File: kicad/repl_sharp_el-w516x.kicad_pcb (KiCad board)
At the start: 2 copper layers, 68.6 x 141.2 mm, 117 parts, among them J1 USB_B_Micro, J3 AVR-ISP-6, SW1 SW_RESET, SW10 SW_Push, SW11 SW_Push, SW12 SW_Push, SW13 SW_Push, SW14 SW_Push, SW15 SW_Push, SW16 SW_Push, SW17 SW_Push, SW18 SW_Push, SW19 SW_Push, SW2 SW_Push, SW20 SW_Push, SW21 SW_Push, SW22 SW_Push, SW23 SW_Push, SW24 SW_Push, SW25 SW_Push, SW26 SW_Push, SW27 SW_Push, SW28 SW_Push, SW29 SW_Push, SW3 SW_Push, SW30 SW_Push, SW31 SW_Push, SW32 SW_Push, SW33 SW_Push, SW34 SW_Push, SW35 SW_Push, SW36 SW_Push, SW37 SW_Push, SW38 SW_Push, SW39 SW_Push, SW4 SW_Push, SW40 SW_Push, SW41 SW_Push, SW42 SW_Push, SW43 SW_Push, SW44 SW_Push, SW45 SW_Push, SW46 SW_Push, SW47 SW_Push, SW48 SW_Push, SW49 SW_Push, SW5 SW_Push, SW50 SW_Push, SW51 SW_Push, SW52 SW_Push, SW53 SW_Push, SW58 SW_POWER, SW6 SW_Push, SW7 SW_Push, SW8 SW_Push, SW9 SW_Push, U1 74HC165D, U2 ATmega32U4-AU, U3 74HC595, U4 BQ24072RGTR, U5 AP2210-33, Y1 Crystal

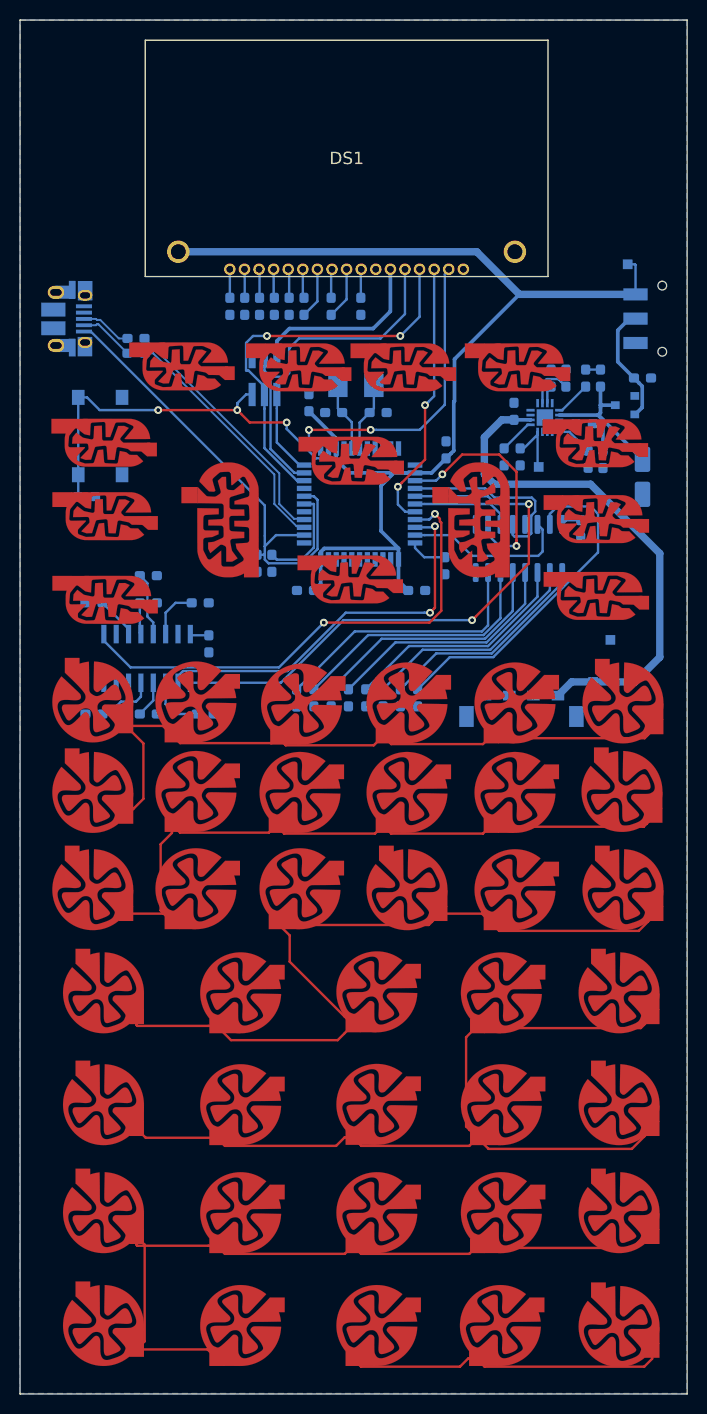
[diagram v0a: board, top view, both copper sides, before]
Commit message: kicad: completed partial layout
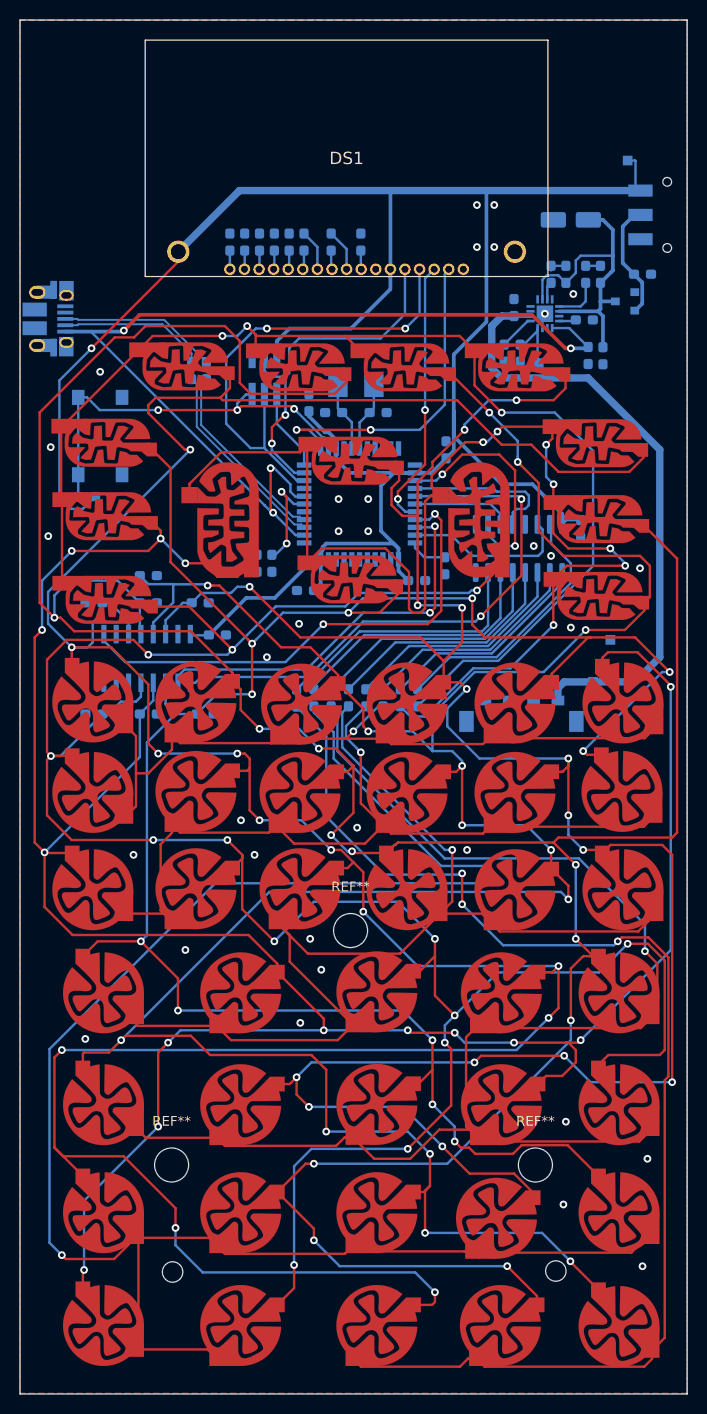
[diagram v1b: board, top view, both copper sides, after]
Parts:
- added REF**: MountingHole_2.1mm, MountingHole:MountingHole_2.1mm, F.Cu at (117.0, 137.5)
- added REF**: MountingHole_3.5mm, MountingHole:MountingHole_3.5mm, F.Cu at (135.3, 102.4)
- added REF**: MountingHole_3.5mm, MountingHole:MountingHole_3.5mm, F.Cu at (116.9, 126.5)
- added REF**: MountingHole_3.5mm, MountingHole:MountingHole_3.5mm, F.Cu at (154.3, 126.5)
- added REF**: MountingHole_2.1mm, MountingHole:MountingHole_2.1mm, F.Cu at (156.4, 137.4)
- moved C22 27.4 mm to (157.9, 29.3), turned to 180 degrees
- moved SW58 10.7 mm to (167.8, 28.8)
- moved C11 10.7 mm to (159.7, 43.3)
- moved C13 10.7 mm to (152.1, 38.4)
- moved C23 10.7 mm to (161.2, 43.3)
- moved C24 10.7 mm to (165.3, 34.9)
- moved D1 10.7 mm to (157.4, 34.9)
- moved D59 10.7 mm to (161.0, 34.9)
- moved R14 10.7 mm to (152.7, 43.0)
- moved R15 10.7 mm to (159.3, 39.6)
- moved R16 10.7 mm to (151.1, 43.0)
- moved R17 10.7 mm to (155.9, 34.9)
- moved R18 10.7 mm to (159.5, 34.9)
- moved TP1 10.7 mm to (163.8, 23.2)
- moved TP5 10.7 mm to (154.6, 44.1)
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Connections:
- net Net-(R2-Pad1) renamed /uD+
- net Net-(R3-Pad1) renamed /uD-
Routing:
- net row0: track 4.32 -> 307.6 mm, vias 0 -> 12
- net row1: track 3.26 -> 292.6 mm, vias 0 -> 11
- net row2: track 6.58 -> 270.8 mm, vias 0 -> 14
- net row5: track 3.79 -> 251.8 mm, vias 0 -> 14
- net row6: track 6.12 -> 245.0 mm, vias 0 -> 13
- net row3: track 5.30 -> 230.8 mm, vias 0 -> 15
- net row4: track 5.81 -> 217.2 mm, vias 0 -> 11
- net Net-(D3-Pad1): track 0.00 -> 128.1 mm, vias 0 -> 7
- net Net-(D2-Pad1): track 0.00 -> 122.2 mm, vias 0 -> 3
- net Net-(D8-Pad1): track 76.8 -> 186.1 mm, vias 0 -> 1
- net Net-(D9-Pad1): track 33.0 -> 130.5 mm, vias 0 -> 3
- net +3V3: track 142.5 -> 227.7 mm, vias 0 -> 1
- net VBUS: track 54.2 -> 109.0 mm, vias 0 -> 4
- net Net-(D7-Pad1): track 87.1 -> 141.2 mm, vias 0 -> 1
- net Net-(D6-Pad1): track 79.4 -> 109.1 mm, vias 0 -> 1
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- added copper zone on F.Cu, net -BATT

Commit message: kicad: finalize design
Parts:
- removed the C14 at (124.4, 31.6)
- removed the C15 at (127.5, 31.6)
- removed the C16 at (136.4, 31.6)
- removed the C17 at (122.9, 31.6)
- removed the C18 at (125.9, 31.6)
- removed the C19 at (129.0, 31.6)
- removed the C20 at (130.5, 31.6)
- removed the C21 at (133.3, 31.6)
- removed the D1 at (157.4, 34.9)
- removed SW11, SW13, SW2: SW_Push, pcb_buttons:btn_rect
- removed SW20, SW27, SW29, SW48, SW49: SW_Push, pcb_buttons:btn_circular
- added C10: 1u, Capacitor_SMD:C_0603_1608Metric_Pad1.05x0.95mm_HandSolder, B.Cu at (133.9, 31.6)
- added C3: 0.1u, Capacitor_SMD:C_0603_1608Metric_Pad1.05x0.95mm_HandSolder, B.Cu at (125.0, 31.6)
- added C4: 0.1u, Capacitor_SMD:C_0603_1608Metric_Pad1.05x0.95mm_HandSolder, B.Cu at (128.1, 31.6)
- added C5: 1u, Capacitor_SMD:C_0603_1608Metric_Pad1.05x0.95mm_HandSolder, B.Cu at (137.0, 31.6)
- added C6: 0.1u, Capacitor_SMD:C_0603_1608Metric_Pad1.05x0.95mm_HandSolder, B.Cu at (123.5, 31.6)
- added C7: 0.1u, Capacitor_SMD:C_0603_1608Metric_Pad1.05x0.95mm_HandSolder, B.Cu at (126.6, 31.6)
- added C8: 0.1u, Capacitor_SMD:C_0603_1608Metric_Pad1.05x0.95mm_HandSolder, B.Cu at (129.6, 31.6)
- added C9: 1u, Capacitor_SMD:C_0603_1608Metric_Pad1.05x0.95mm_HandSolder, B.Cu at (131.1, 31.6)
- added D11: LED, Diode_SMD:D_0603_1608Metric_Pad1.05x0.95mm_HandSolder, B.Cu at (145.6, 48.7)
- added D9: LED_PGOOD, LED_SMD:LED_0603_1608Metric_Pad1.05x0.95mm_HandSolder, B.Cu at (156.4, 33.7)
- added G***: LOGO, pcb_buttons:board, F.Cu at (135.3, 94.9)
- added R12: 10k, Resistor_SMD:R_0603_1608Metric_Pad1.05x0.95mm_HandSolder, B.Cu at (107.7, 74.3)
- added R15: 1k, Resistor_SMD:R_0603_1608Metric_Pad1.05x0.95mm_HandSolder, B.Cu at (159.2, 34.9)
- added REF**: MountingHole_2.1mm, MountingHole:MountingHole_2.1mm, F.Cu at (152.8, 50.3)
- added REF**: MountingHole_2.1mm, MountingHole:MountingHole_2.1mm, F.Cu at (117.7, 49.8)
- added SW54: SW_Push, pcb_buttons:btn_circular, F.Cu at (152.1, 88.0)
- added SW55: SW_Push, pcb_buttons:btn_circular, F.Cu at (163.3, 88.0)
- added SW58: SW_Push, pcb_buttons:btn_circular, F.Cu at (108.7, 78.9)
- added SW59: SW_Push, pcb_buttons:btn_circular, F.Cu at (119.3, 78.9)
- added SW60: SW_Push, pcb_buttons:btn_circular, F.Cu at (130.0, 78.9)
- added SW61: SW_Push, pcb_buttons:btn_circular, F.Cu at (140.9, 78.9)
- added SW62: SW_Push, pcb_buttons:btn_circular, F.Cu at (152.1, 78.9)
- added SW63: SW_Push, pcb_buttons:btn_circular, F.Cu at (163.3, 78.9)
- SW12: footprint pcb_buttons:btn_rect -> pcb_buttons:btn_long_rect
- SW14, SW15: footprint pcb_buttons:btn_long_rect -> pcb_buttons:btn_circular
- SW18, SW19, SW21, SW26, SW34, SW35, SW36, SW37: footprint pcb_buttons:btn_circular -> pcb_buttons:btn_rect
- SW28: footprint pcb_buttons:btn_circular -> pcb_buttons:btn_long_rect
- SW6, SW7, SW8, SW9: footprint pcb_buttons:btn_rect -> pcb_buttons:btn_circular
- moved SW9 104.0 mm to (109.9, 143.0), turned to 270 degrees
- moved SW34 77.5 mm to (152.9, 44.3), turned to 0 degrees
- moved SW35 67.5 mm to (161.0, 52.3)
- moved SW15 64.9 mm to (123.9, 120.3)
- moved SW17 64.3 mm to (123.9, 143.0), turned to 270 degrees
- moved SW8 63.0 mm to (109.9, 131.4), turned to 270 degrees
- moved SW7 60.5 mm to (109.9, 120.3), turned to 90 degrees
- moved SW53 59.3 mm to (140.9, 88.0), turned to 0 degrees
- moved SW52 58.6 mm to (130.0, 88.1)
- moved SW51 57.8 mm to (119.3, 88.3)
- moved SW50 56.9 mm to (108.8, 88.1)
- moved SW6 56.6 mm to (109.8, 108.8), turned to 270 degrees
- moved SW28 55.0 mm to (148.5, 60.2)
- moved SW25 54.8 mm to (137.9, 142.9), turned to 270 degrees
- moved SW16 54.7 mm to (123.9, 131.4), turned to 270 degrees
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- renumbered C2 to C1, C8 to C11, C9 to C13, C10 to C14, C1 to C15, C3 to C16, C5 to C17, C6 to C18, C13 to C19, C4 to C2, C22 to C20, C23 to C21, C11 to C22, C24 to C23, D2 to D1, D59 to D10, D3 to D2, D4 to D3, D5 to D4, D6 to D5, D7 to D6, D8 to D7, D9 to D8, J3 to J2, R11 to R10, R12 to R11, R16 to R13, R17 to R14, R14 to R16, R15 to R17, R5 to R4, R6 to R5, R7 to R6, R8 to R7, R9 to R8, R10 to R9, SW58 to SW66, TP4 to TP3, TP5 to TP4
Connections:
- C1 pad 2: -BATT -> GND
- C11 pad 2: -BATT -> GND
- C12 pad 1: -BATT -> GND
- C13 pad 2: -BATT -> GND
- C14 pad 1: -BATT -> GND
- C15 pad 2: -BATT -> GND
- C16 pad 2: -BATT -> GND
- C17 pad 2: -BATT -> GND
- C18 pad 2: -BATT -> GND
- C19 pad 1: -BATT -> GND
- C2 pad 2: -BATT -> GND
- C20 pad 2: -BATT -> GND
- C21 pad 2: -BATT -> GND
- C22 pad 1: -BATT -> GND
- C23 pad 2: -BATT -> GND
- D1 pad 1: Net-(D2-Pad1) -> Net-(D1-Pad1)
- D10 pad 1: Net-(D59-Pad1) -> Net-(D10-Pad1)
- D2 pad 1: Net-(D3-Pad1) -> Net-(D2-Pad1)
- D3 pad 1: Net-(D4-Pad1) -> Net-(D3-Pad1)
- D4 pad 1: Net-(D5-Pad1) -> Net-(D4-Pad1)
- D5 pad 1: Net-(D6-Pad1) -> Net-(D5-Pad1)
- D6 pad 1: Net-(D7-Pad1) -> Net-(D6-Pad1)
- D7 pad 1: Net-(D8-Pad1) -> Net-(D7-Pad1)
- D8 pad 1: Net-(D9-Pad1) (its old number) -> Net-(D8-Pad1)
- DS1 pad 11: -BATT -> GND
- DS1 pad 17: -BATT -> GND
- DS1 pad MH2: -BATT -> GND
- J1 pad 5: -BATT -> GND
- J1 pad 6: -BATT -> GND
- J2 pad 6: -BATT -> GND
- R10 pad 1: -BATT -> GND
- R11 pad 1: -BATT -> GND
- R13 pad 1: -BATT -> GND
- R16 pad 2: -BATT -> GND
- R17 pad 2: -BATT -> GND
- R18 pad 1: Net-(D59-Pad1) -> Net-(D11-Pad1)
- R18 pad 2: Net-(R18-Pad2) -> GND
- R4 pad 1: -BATT -> GND
- R5 pad 1: -BATT -> GND
- R6 pad 1: -BATT -> GND
- R7 pad 1: -BATT -> GND
- R8 pad 1: -BATT -> GND
- R9 pad 1: -BATT -> GND
- SW1 pad 1: -BATT -> GND
- SW10 pad 1: row1 -> row0
- SW10 pad 2: Net-(D3-Pad1) -> Net-(D2-Pad1)
- SW12 pad 1: row3 -> row2
- SW12 pad 2: Net-(D3-Pad1) -> Net-(D2-Pad1)
- SW14 pad 1: row5 -> row4
- SW14 pad 2: Net-(D3-Pad1) -> Net-(D2-Pad1)
- SW15 pad 1: row6 -> row5
- SW15 pad 2: Net-(D3-Pad1) -> Net-(D2-Pad1)
- SW16 pad 1: row0 -> row6
- SW16 pad 2: Net-(D4-Pad1) -> Net-(D2-Pad1)
- SW17 pad 1: row1 -> row7
- SW17 pad 2: Net-(D4-Pad1) -> Net-(D2-Pad1)
- SW18 pad 1: row2 -> row0
- SW18 pad 2: Net-(D4-Pad1) -> Net-(D3-Pad1)
- SW19 pad 1: row3 -> row1
- SW19 pad 2: Net-(D4-Pad1) -> Net-(D3-Pad1)
- SW21 pad 1: row5 -> row3
- SW21 pad 2: Net-(D4-Pad1) -> Net-(D3-Pad1)
- SW22 pad 1: row6 -> row4
- SW22 pad 2: Net-(D4-Pad1) -> Net-(D3-Pad1)
- SW23 pad 1: row0 -> row5
- SW23 pad 2: Net-(D5-Pad1) -> Net-(D3-Pad1)
- SW24 pad 1: row1 -> row6
- SW24 pad 2: Net-(D5-Pad1) -> Net-(D3-Pad1)
- SW25 pad 1: row2 -> row7
- SW25 pad 2: Net-(D5-Pad1) -> Net-(D3-Pad1)
- SW26 pad 1: row3 -> row0
- SW26 pad 2: Net-(D5-Pad1) -> Net-(D4-Pad1)
- SW28 pad 1: row5 -> row2
- SW28 pad 2: Net-(D5-Pad1) -> Net-(D4-Pad1)
- SW3 pad 2: Net-(D2-Pad1) -> Net-(D1-Pad1)
- SW30 pad 1: row0 -> row4
- SW30 pad 2: Net-(D6-Pad1) -> Net-(D4-Pad1)
- SW31 pad 1: row1 -> row5
- SW31 pad 2: Net-(D6-Pad1) -> Net-(D4-Pad1)
- SW32 pad 1: row2 -> row6
- SW32 pad 2: Net-(D6-Pad1) -> Net-(D4-Pad1)
- SW33 pad 1: row3 -> row7
- SW33 pad 2: Net-(D6-Pad1) -> Net-(D4-Pad1)
- SW34 pad 1: row4 -> row0
- SW34 pad 2: Net-(D6-Pad1) -> Net-(D5-Pad1)
- SW35 pad 1: row5 -> row1
- SW35 pad 2: Net-(D6-Pad1) -> Net-(D5-Pad1)
- SW36 pad 1: row6 -> row2
- SW36 pad 2: Net-(D6-Pad1) -> Net-(D5-Pad1)
- SW37 pad 1: row0 -> row3
- SW37 pad 2: Net-(D7-Pad1) -> Net-(D5-Pad1)
- SW38 pad 1: row1 -> row4
- SW38 pad 2: Net-(D7-Pad1) -> Net-(D5-Pad1)
- SW39 pad 1: row2 -> row5
- SW39 pad 2: Net-(D7-Pad1) -> Net-(D5-Pad1)
- SW4 pad 2: Net-(D2-Pad1) -> Net-(D1-Pad1)
- SW40 pad 1: row3 -> row6
- SW40 pad 2: Net-(D7-Pad1) -> Net-(D5-Pad1)
- SW41 pad 1: row4 -> row7
- SW41 pad 2: Net-(D7-Pad1) -> Net-(D5-Pad1)
- SW42 pad 1: row5 -> row0
- SW42 pad 2: Net-(D7-Pad1) -> Net-(D6-Pad1)
- SW43 pad 1: row6 -> row1
- SW43 pad 2: Net-(D7-Pad1) -> Net-(D6-Pad1)
- SW44 pad 1: row0 -> row2
- SW44 pad 2: Net-(D8-Pad1) -> Net-(D6-Pad1)
- SW45 pad 1: row1 -> row3
- SW45 pad 2: Net-(D8-Pad1) -> Net-(D6-Pad1)
- SW46 pad 1: row2 -> row4
- SW46 pad 2: Net-(D8-Pad1) -> Net-(D6-Pad1)
- SW47 pad 1: row3 -> row5
- SW47 pad 2: Net-(D8-Pad1) -> Net-(D6-Pad1)
- SW5 pad 2: Net-(D2-Pad1) -> Net-(D1-Pad1)
- SW50 pad 1: row6 -> row0
- SW50 pad 2: Net-(D8-Pad1) -> Net-(D7-Pad1)
- SW51 pad 1: row0 -> row1
- SW51 pad 2: Net-(D9-Pad1) (its old number) -> Net-(D7-Pad1)
- SW52 pad 1: row1 -> row2
- SW52 pad 2: Net-(D9-Pad1) (its old number) -> Net-(D7-Pad1)
- SW53 pad 1: row2 -> row3
- SW53 pad 2: Net-(D9-Pad1) (its old number) -> Net-(D7-Pad1)
- SW6 pad 2: Net-(D2-Pad1) -> Net-(D1-Pad1)
- SW7 pad 2: Net-(D2-Pad1) -> Net-(D1-Pad1)
- SW8 pad 2: Net-(D2-Pad1) -> Net-(D1-Pad1)
- SW9 pad 1: row0 -> row7
- SW9 pad 2: Net-(D3-Pad1) -> Net-(D1-Pad1)
- TP2 pad 1: -BATT -> GND
- U1 pad 10: -BATT -> GND
- U1 pad 15: -BATT -> GND
- U1 pad 6: -BATT -> row7
- U1 pad 8: -BATT -> GND
- U2 pad 15: -BATT -> GND
- U2 pad 23: -BATT -> GND
- U2 pad 35: -BATT -> GND
- U2 pad 43: -BATT -> GND
- U2 pad 5: -BATT -> GND
- U3 pad 13: -BATT -> GND
- U3 pad 8: -BATT -> GND
- U4 pad 15: -BATT -> GND
- U4 pad 17: -BATT -> GND
- U4 pad 4: -BATT -> GND
- U4 pad 5: -BATT -> GND
- U4 pad 8: -BATT -> GND
- U4 pad 9: Net-(R18-Pad2) -> Net-(R15-Pad2)
- U5 pad 1: -BATT -> GND
- XB1 pad 3: -BATT -> GND
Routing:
- net Net-(D1-Pad1): track 0.00 -> 173.2 mm, vias 0 -> 5
- net row0: track 307.6 -> 163.7 mm, vias 12 -> 3
- net row1: track 292.6 -> 151.2 mm
- net row7: track 0.00 -> 139.8 mm, vias 0 -> 1
- net row2: track 270.8 -> 131.8 mm, vias 14 -> 5
- net Net-(D9-Pad1) (its old number): track 130.5 -> 0.00 mm, vias 3 -> 0
- net row3: track 230.8 -> 101.8 mm, vias 15 -> 11
- net Net-(D8-Pad1): track 186.1 -> 62.6 mm
- net row6: track 245.0 -> 122.6 mm, vias 13 -> 1
- net row5: track 251.8 -> 142.7 mm, vias 14 -> 1
- net Net-(D4-Pad1): track 73.9 -> 180.9 mm, vias 1 -> 6
- net Net-(D5-Pad1): track 83.8 -> 183.2 mm, vias 1 -> 6
- net Net-(D2-Pad1): track 122.2 -> 198.2 mm, vias 3 -> 9
- net row4: track 217.2 -> 142.9 mm, vias 11 -> 7
- net Net-(D7-Pad1): track 141.2 -> 73.9 mm
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- added copper zone on B.Cu, net GND
- added copper zone on F.Cu, net GND
- removed copper zone on B.Cu, net -BATT
- removed copper zone on F.Cu, net -BATT
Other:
- board text added: "SHARP_EL-W516X"
- board text added: "auxillary modification board 0.0.1 (c) 2019 netdex"

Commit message: kicad: design after production
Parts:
- added JP1: Jumper_2_Open, Jumper:SolderJumper-2_P1.3mm_Open_Pad1.0x1.5mm, B.Cu at (136.4, 68.1)
- U1: value 74HC165D -> SOIC-16_3.9x9.9mm_P1.27mm; footprint footprints:74HC165D -> Package_SO:SOIC-16_3.9x9.9mm_P1.27mm
- moved TP1 5.16 mm to (158.7, 24.1)
- moved TP3 2.64 mm to (161.8, 74.7)
- moved R13 1.31 mm to (152.2, 42.4)
- moved R2 0.89 mm to (121.7, 44.9)
- moved R3 0.89 mm to (120.2, 44.9)
- moved TP4 0.85 mm to (154.1, 43.8)
- moved TP2 0.80 mm to (161.8, 71.8)
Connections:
- R4 pad 1: GND -> +3V3
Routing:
- net Net-(JP1-Pad1): track 3.98 -> 17.4 mm
- net +3V3: track 225.4 -> 230.1 mm
- net VBUS: track 111.0 -> 109.8 mm
- net Net-(D1-Pad1): track 173.2 -> 174.4 mm
- net /uc_n_reset: track 43.0 -> 44.2 mm
- net Net-(C23-Pad1): track 11.3 -> 12.3 mm
- net Net-(R13-Pad2): track 3.72 -> 2.73 mm
- net +BATT: track 60.5 -> 61.5 mm
- net Net-(R16-Pad1): track 4.26 -> 5.19 mm
- net /D+: track 18.6 -> 17.7 mm
- net /D-: track 17.4 -> 16.5 mm
- net row5: track 142.7 -> 143.5 mm
- net row3: track 101.8 -> 102.6 mm
- net Net-(D4-Pad1): track 180.9 -> 181.5 mm
- net col0: track 27.2 -> 27.7 mm
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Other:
- rule solder_mask_min_width: 0.25 -> 0.08

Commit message: kicad: finalize device BOM
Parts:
- U1: value SOIC-16_3.9x9.9mm_P1.27mm -> 74HC165D
